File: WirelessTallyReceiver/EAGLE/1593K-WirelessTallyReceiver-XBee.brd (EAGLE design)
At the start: 80.7 x 51.5 mm, 16 parts, among them IC1 75176AP, J1 RJHSE-5381

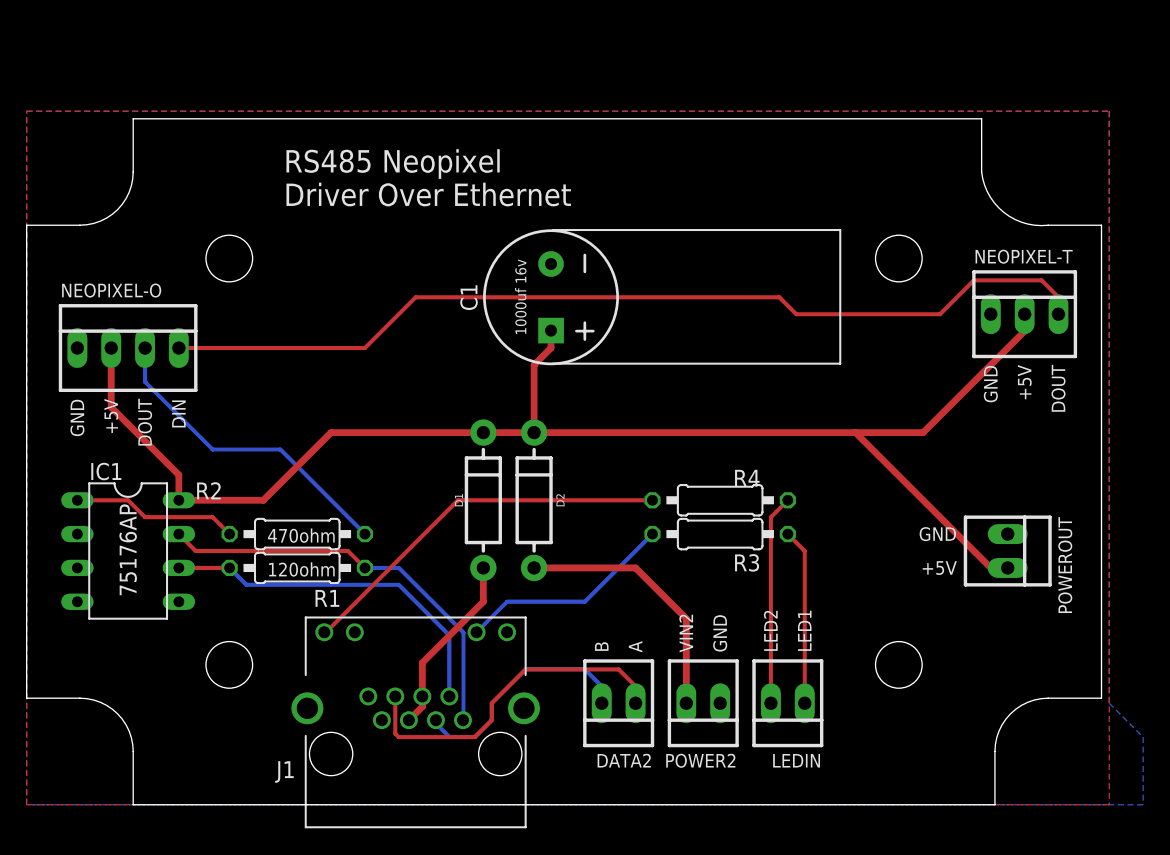
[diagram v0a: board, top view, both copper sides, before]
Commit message: Revisions to boards after working with initial prototypes.
- Update boards to use SMD components to help save on space.
- Redesign wireless receiver to use 3.3v logic to avoid using the Xbee breakout.
- Remove designs that aren't going to be used.
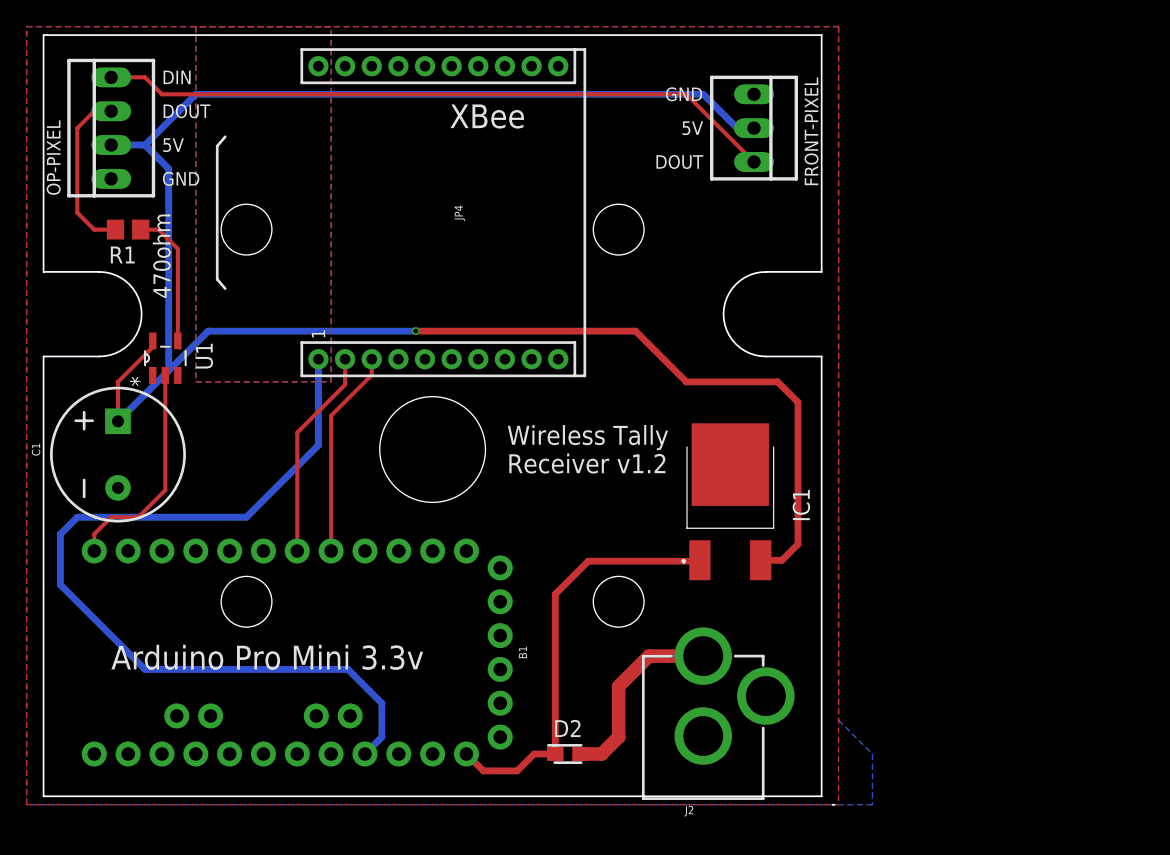
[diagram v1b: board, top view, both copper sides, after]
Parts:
- removed D1: 1A/50V/1.1V, SparkFun-DiscreteSemi:DIODE-1N4001
- removed DATA2, LEDIN, POWER2, POWEROUT: 22-23-2021, con-molex:22-23-2021
- removed J1: RJHSE-5381, RJHSE-5381:AMPHENOL_RJHSE-5381
- removed NEOPIXEL-O: 22-23-2041, con-molex:22-23-2041
- removed NEOPIXEL-T: 22-23-2031, con-molex:22-23-2031
- removed R2: 470ohm, rcl:0207/10
- removed R3, R4: (no value), rcl:0207/10
- added B1: ARDUINO_PRO_MINI, SparkFun-Boards:ARDUINO_PRO_MINI
- added FRONT-PIXEL: 22-23-2031, con-molex:22-23-2031
- added J2: POWER_JACK, SparkFun-Connectors:POWER_JACK_PTH
- added JP4: (no value), SparkFun-RF:XBEE-SILK
- added OP-PIXEL: 22-23-2041, con-molex:22-23-2041
- added U1: SN74AHCT1G125DBVR, Texas Instruments_By_element14_Batch_1:SOT95P280X145-5N
- C1: value 1000uf 16v -> 1000uf
- D2: value 1A/50V/1.1V -> ACDBS140-HF; device SparkFun-DiscreteSemi:DIODE-1N4001 -> SamacSys_Parts:DIOM2013X100N
- IC1: value 75176AP -> NCP5501DT50RKG; device 751xx:DIL08 -> SamacSys_Parts:NCP5501DT50RKG
- R1: value 120ohm -> 470ohm; device rcl:0207/10 -> rcl:R0805
- U$1: device hammond:1591XXM -> hammond-box1:1593K
- moved IC1 45.4 mm to (52.8, 22.6)
- moved U$1 42.2 mm to (30.5, 29.2)
- moved C1 34.6 mm to (6.86, 26.3), turned to 90 degrees
- moved R1 28.4 mm to (7.62, 43.2), turned to 180 degrees
- moved D2 19.2 mm to (40.6, 3.81), turned to 0 degrees
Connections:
- removed net DATA1A: IC1.6, J1.2, R1.1
- removed net DATA1B: IC1.7, J1.1, R1.2
- removed net DATA2A: DATA2.1, J1.6
- removed net DATA2B: DATA2.2, J1.3
- removed net LED1: J1.10, R3.2
- removed net LED1IN: LEDIN.1, R3.1
- removed net LED2: J1.12, R4.2
- removed net LED2IN: LEDIN.2, R4.1
- removed net NEO-O: NEOPIXEL-O.3, R2.2
- removed net NEO-T: NEOPIXEL-O.4, NEOPIXEL-T.3
- removed net NEODATA: IC1.1, R2.1
- removed net VCC: C1.+, D1.C, D2.C, IC1.8, NEOPIXEL-O.2, NEOPIXEL-T.2, POWEROUT.2
- removed net VIN1: D1.A, J1.4, J1.5
- removed net VIN2: D2.A, POWER2.2
- new net 3.3V: B1.21, JP4.1
- new net 5V: C1.+, FRONT-PIXEL.2, IC1.3, OP-PIXEL.2, U1.5
- new net DIN: B1.5, JP4.3
- new net DOUT: B1.6, JP4.2
- new net NEOCROSS: FRONT-PIXEL.3, OP-PIXEL.4
- new net NEOOUT: OP-PIXEL.3, R1.2
- new net NEOOUT3V: B1.12, U1.2
- new net NEOPIXEL: R1.1, U1.4
- new net PWR: D2.2, J2.PWR
- new net RESET: B1.22
- new net VIN: B1.24, D2.1, IC1.1
- net GND: now also B1.23, B1.4, FRONT-PIXEL.1, J2.GND, J2.GNDBREAK, JP4.10, OP-PIXEL.1, U1.1, U1.3; no longer IC1.3, IC1.4, IC1.5, J1.11, J1.7, J1.8, J1.9, J1.S1, J1.S2, NEOPIXEL-O.1, NEOPIXEL-T.1, POWER2.1, POWEROUT.1
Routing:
- net 5V: track 0.00 -> 145.7 mm, vias 0 -> 1
- net VCC: track 107.4 -> 0.00 mm
- net NEO-T: track 71.0 -> 0.00 mm
- net 3.3V: track 0.00 -> 64.6 mm
- net NEOCROSS: track 0.00 -> 50.9 mm
- net VIN: track 0.00 -> 31.6 mm
- net DATA1B: track 31.0 -> 0.00 mm
- net LED2: track 28.7 -> 0.00 mm
- net DATA1A: track 27.0 -> 0.00 mm
- net DATA2A: track 25.6 -> 0.00 mm
- net NEO-O: track 23.8 -> 0.00 mm
- net VIN2: track 19.4 -> 0.00 mm
- net DATA2B: track 17.8 -> 0.00 mm
- net NEOOUT3V: track 0.00 -> 16.6 mm
- net LED1: track 16.3 -> 0.00 mm
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- added copper zone on layer 16, net N$1
- added copper zone on layer 1, net N$2
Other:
- board size 80.7 x 51.5 mm -> 59.4 x 57.8 mm
- board text added: "5V"
- board text added: "Arduino Pro Mini 3.3v"
- board text added: "Fits Hammond 1593K"
- board text added: "Wireless Tally Receiver v1.2"
- board text added: "XBee"
- board text removed: "+5V"
- board text removed: "A"
- board text removed: "B"
- board text removed: "Fits Hammond 1591XXM"
- board text removed: "LED1"
- board text removed: "LED2"
- board text removed: "RS485 Neopixel Driver Over Ethernet"
- board text removed: "VIN2"

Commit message: Add decoupling caps
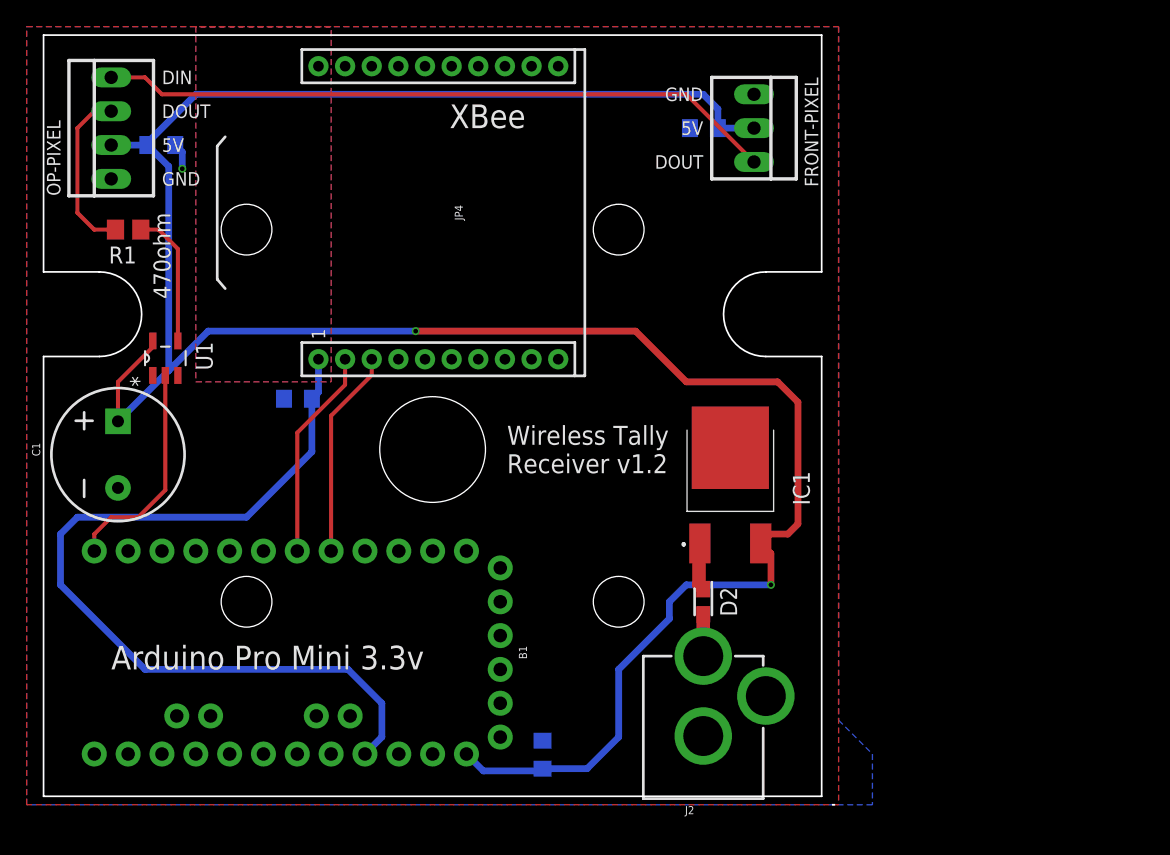
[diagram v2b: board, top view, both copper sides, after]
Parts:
- added C2, C3, C4, C5: (no value), Nordic_nRF:RESC0805_N
- moved D2 15.3 mm to (50.8, 15.2), turned to 270 degrees
- moved IC1 1.27 mm to (52.8, 23.9)
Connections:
- net 3.3V: now also C3.1
- net 5V: now also B1.24, C2.1, C4.1, C5.1
- net GND: now also C2.2, C3.2, C4.2, C5.2
- net VIN: no longer B1.24
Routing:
- net 5V: track 145.7 -> 181.5 mm, vias 1 -> 2
- net VIN: track 31.6 -> 3.60 mm
- net PWR: track 14.5 -> 3.13 mm
- net GND: track 0.00 -> 2.00 mm, vias 0 -> 1
